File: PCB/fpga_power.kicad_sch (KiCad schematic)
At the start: 6 parts, among them U4 LFE5U-25F-6BG256C

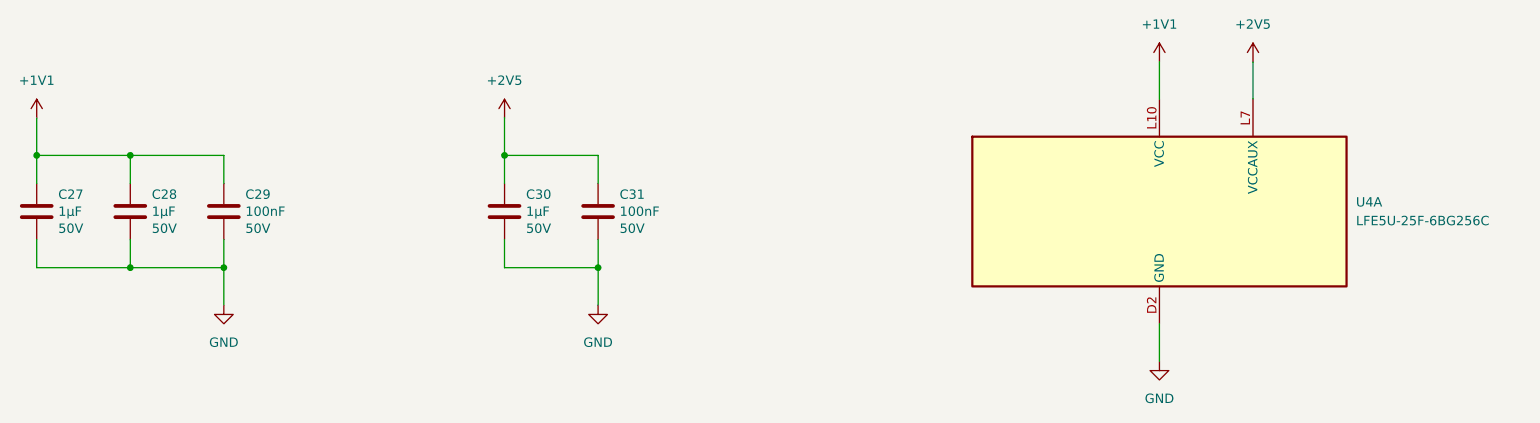
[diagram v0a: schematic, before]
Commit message: Add ESD protection
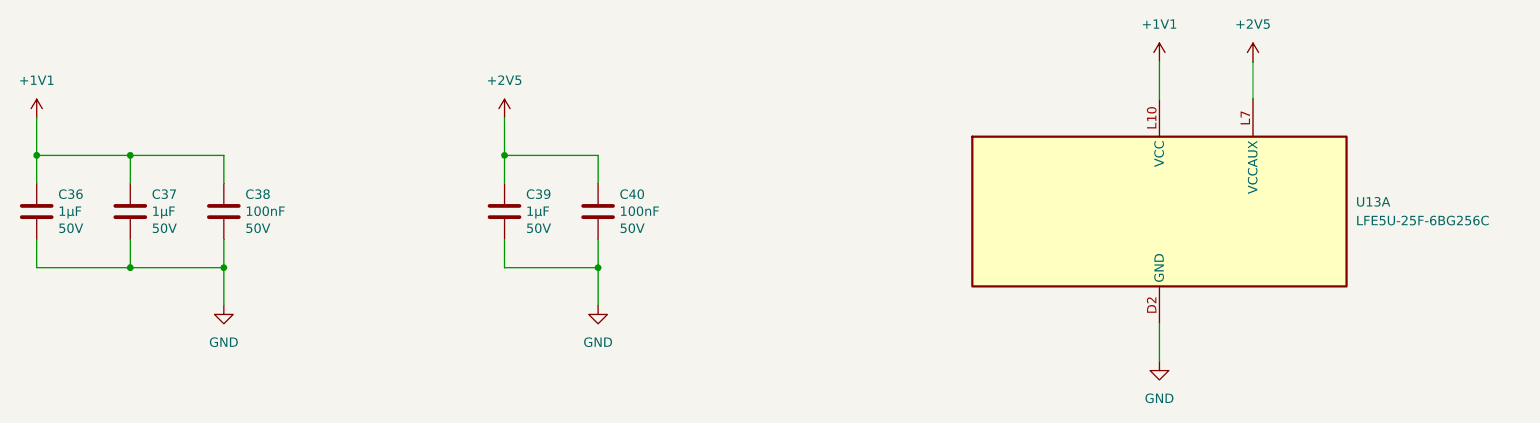
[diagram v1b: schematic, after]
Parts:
- renumbered C27 to C36, C28 to C37, C29 to C38, C30 to C39, C31 to C40, U4 to U13
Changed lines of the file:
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@@
 	(title_block
 		(title "Clavier - FPGA power")
-		(date "2025-06-01")
+		(date "2025-06-21")
 		(rev "1.0")
 		(company "Copyright (c) 2025 L. Sartory")
@@
 		(on_board yes)
 		(dnp no)
-		(property "Reference" "C27"
+		(property "Reference" "C36"
 			(at 53.721 86.5886 0)
 			(effects
@@
 			(project "clavier"
 				(path "/6362c6e0-59ef-40d3-b6e0-7e9dfe7b9b20/d73938da-f0ba-48e3-aac9-a36988c25c2c/e36c52fe-7af8-49a0-bf3c-a636c30fc9cb"
-					(reference "C27")
+					(reference "C36")
 					(unit 1)
 				)
@@
 		(on_board yes)
 		(dnp no)
-		(property "Reference" "C29"
+		(property "Reference" "C38"
 			(at 79.121 86.5886 0)
 			(effects
@@
 			(project "clavier"
 				(path "/6362c6e0-59ef-40d3-b6e0-7e9dfe7b9b20/d73938da-f0ba-48e3-aac9-a36988c25c2c/e36c52fe-7af8-49a0-bf3c-a636c30fc9cb"
-					(reference "C29")
+					(reference "C38")
 					(unit 1)
 				)
@@
 		(on_board yes)
 		(dnp no)
-		(property "Reference" "C28"
+		(property "Reference" "C37"
 			(at 66.421 86.5886 0)
 			(effects
@@
 			(project "clavier"
 				(path "/6362c6e0-59ef-40d3-b6e0-7e9dfe7b9b20/d73938da-f0ba-48e3-aac9-a36988c25c2c/e36c52fe-7af8-49a0-bf3c-a636c30fc9cb"
-					(reference "C28")
+					(reference "C37")
 					(unit 1)
 				)
@@
 		(on_board yes)
 		(dnp no)
-		(property "Reference" "C30"
+		(property "Reference" "C39"
 			(at 117.221 86.5886 0)
 			(effects
@@
 			(project "clavier"
 				(path "/6362c6e0-59ef-40d3-b6e0-7e9dfe7b9b20/d73938da-f0ba-48e3-aac9-a36988c25c2c/e36c52fe-7af8-49a0-bf3c-a636c30fc9cb"
-					(reference "C30")
+					(reference "C39")
 					(unit 1)
 				)
@@
 		(dnp no)
 		(fields_autoplaced yes)
-		(property "Reference" "U4"
+		(property "Reference" "U13"
 			(at 229.87 87.6299 0)
 			(effects
@@
 			(project "clavier"
 				(path "/6362c6e0-59ef-40d3-b6e0-7e9dfe7b9b20/d73938da-f0ba-48e3-aac9-a36988c25c2c/e36c52fe-7af8-49a0-bf3c-a636c30fc9cb"
-					(reference "U4")
+					(reference "U13")
 					(unit 1)
 				)
@@
 		(dnp no)
 		(fields_autoplaced yes)
-		(property "Reference" "#PWR057"
+		(property "Reference" "#PWR076"
 			(at 114.3 80.01 0)
 			(effects
@@
 			(project "clavier"
 				(path "/6362c6e0-59ef-40d3-b6e0-7e9dfe7b9b20/d73938da-f0ba-48e3-aac9-a36988c25c2c/e36c52fe-7af8-49a0-bf3c-a636c30fc9cb"
-					(reference "#PWR057")
+					(reference "#PWR076")
 					(unit 1)
 				)
@@
 		(dnp no)
 		(fields_autoplaced yes)
-		(property "Reference" "#PWR055"
+		(property "Reference" "#PWR074"
 			(at 215.9 72.39 0)
 			(effects
@@
 			(project "clavier"
 				(path "/6362c6e0-59ef-40d3-b6e0-7e9dfe7b9b20/d73938da-f0ba-48e3-aac9-a36988c25c2c/e36c52fe-7af8-49a0-bf3c-a636c30fc9cb"
-					(reference "#PWR055")
+					(reference "#PWR074")
 					(unit 1)
 				)
@@
 		(dnp no)
 		(fields_autoplaced yes)
-		(property "Reference" "#PWR054"
+		(property "Reference" "#PWR073"
 			(at 203.2 72.39 0)
 			(effects
@@
 			(project "clavier"
 				(path "/6362c6e0-59ef-40d3-b6e0-7e9dfe7b9b20/d73938da-f0ba-48e3-aac9-a36988c25c2c/e36c52fe-7af8-49a0-bf3c-a636c30fc9cb"
-					(reference "#PWR054")
+					(reference "#PWR073")
 					(unit 1)
 				)
@@
 		(dnp no)
 		(fields_autoplaced yes)
-		(property "Reference" "#PWR059"
+		(property "Reference" "#PWR078"
 			(at 127 107.95 0)
 			(effects
@@
 			(project "clavier"
 				(path "/6362c6e0-59ef-40d3-b6e0-7e9dfe7b9b20/d73938da-f0ba-48e3-aac9-a36988c25c2c/e36c52fe-7af8-49a0-bf3c-a636c30fc9cb"
-					(reference "#PWR059")
+					(reference "#PWR078")
 					(unit 1)
 				)
@@
 		(dnp no)
 		(fields_autoplaced yes)
-		(property "Reference" "#PWR058"
+		(property "Reference" "#PWR077"
 			(at 76.2 107.95 0)
 			(effects
@@
 			(project "clavier"
 				(path "/6362c6e0-59ef-40d3-b6e0-7e9dfe7b9b20/d73938da-f0ba-48e3-aac9-a36988c25c2c/e36c52fe-7af8-49a0-bf3c-a636c30fc9cb"
-					(reference "#PWR058")
+					(reference "#PWR077")
 					(unit 1)
 				)
@@
 		(dnp no)
 		(fields_autoplaced yes)
-		(property "Reference" "#PWR056"
+		(property "Reference" "#PWR075"
 			(at 50.8 80.01 0)
 			(effects
@@
 			(project "clavier"
 				(path "/6362c6e0-59ef-40d3-b6e0-7e9dfe7b9b20/d73938da-f0ba-48e3-aac9-a36988c25c2c/e36c52fe-7af8-49a0-bf3c-a636c30fc9cb"
-					(reference "#PWR056")
+					(reference "#PWR075")
 					(unit 1)
 				)
@@
 		(dnp no)
 		(fields_autoplaced yes)
-		(property "Reference" "#PWR060"
+		(property "Reference" "#PWR079"
 			(at 203.2 115.57 0)
 			(effects
@@
 			(project "clavier"
 				(path "/6362c6e0-59ef-40d3-b6e0-7e9dfe7b9b20/d73938da-f0ba-48e3-aac9-a36988c25c2c/e36c52fe-7af8-49a0-bf3c-a636c30fc9cb"
-					(reference "#PWR060")
+					(reference "#PWR079")
 					(unit 1)
 				)
@@
 		(on_board yes)
 		(dnp no)
-		(property "Reference" "C31"
+		(property "Reference" "C40"
 			(at 129.921 86.5886 0)
 			(effects
@@
 			(project "clavier"
 				(path "/6362c6e0-59ef-40d3-b6e0-7e9dfe7b9b20/d73938da-f0ba-48e3-aac9-a36988c25c2c/e36c52fe-7af8-49a0-bf3c-a636c30fc9cb"
-					(reference "C31")
+					(reference "C40")
 					(unit 1)
 				)

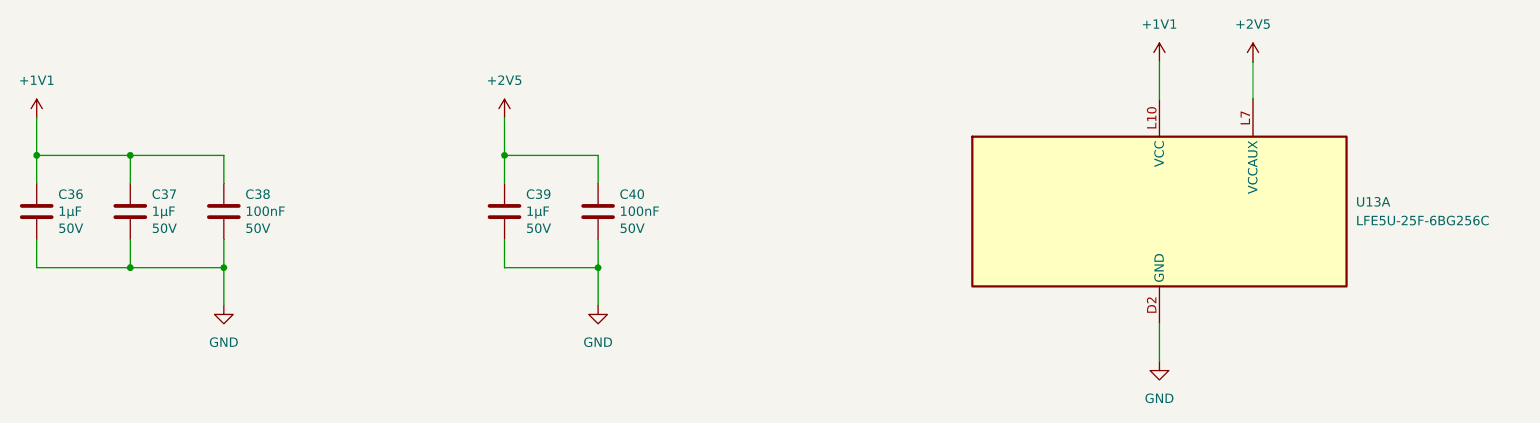
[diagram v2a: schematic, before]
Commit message: Complete the PCB routing
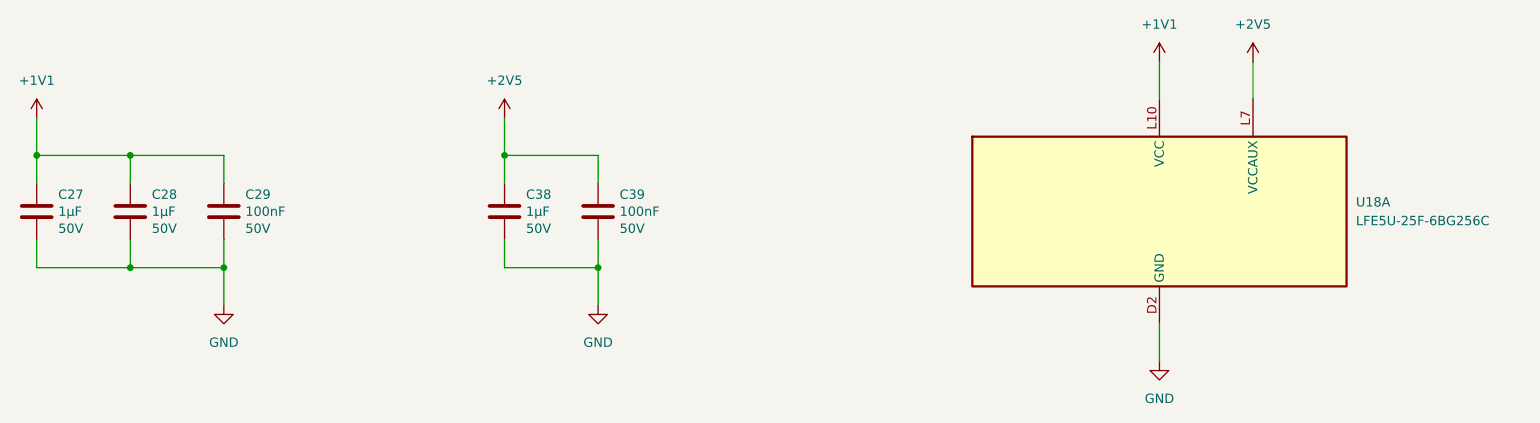
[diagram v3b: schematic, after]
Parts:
- renumbered C36 to C27, C37 to C28, C38 to C29, C39 to C38, C40 to C39, U13 to U18
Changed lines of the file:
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@@
 	(title_block
 		(title "Clavier - FPGA power")
-		(date "2025-06-21")
+		(date "2025-06-22")
 		(rev "1.0")
 		(company "Copyright (c) 2025 L. Sartory")
@@
 		(on_board yes)
 		(dnp no)
-		(property "Reference" "C36"
+		(property "Reference" "C27"
 			(at 53.721 86.5886 0)
 			(effects
@@
 			(project "clavier"
 				(path "/6362c6e0-59ef-40d3-b6e0-7e9dfe7b9b20/d73938da-f0ba-48e3-aac9-a36988c25c2c/e36c52fe-7af8-49a0-bf3c-a636c30fc9cb"
-					(reference "C36")
+					(reference "C27")
 					(unit 1)
 				)
@@
 		(on_board yes)
 		(dnp no)
-		(property "Reference" "C38"
+		(property "Reference" "C29"
 			(at 79.121 86.5886 0)
 			(effects
@@
 			(project "clavier"
 				(path "/6362c6e0-59ef-40d3-b6e0-7e9dfe7b9b20/d73938da-f0ba-48e3-aac9-a36988c25c2c/e36c52fe-7af8-49a0-bf3c-a636c30fc9cb"
-					(reference "C38")
+					(reference "C29")
 					(unit 1)
 				)
@@
 		(on_board yes)
 		(dnp no)
-		(property "Reference" "C37"
+		(property "Reference" "C28"
 			(at 66.421 86.5886 0)
 			(effects
@@
 			(project "clavier"
 				(path "/6362c6e0-59ef-40d3-b6e0-7e9dfe7b9b20/d73938da-f0ba-48e3-aac9-a36988c25c2c/e36c52fe-7af8-49a0-bf3c-a636c30fc9cb"
-					(reference "C37")
+					(reference "C28")
 					(unit 1)
 				)
@@
 		(on_board yes)
 		(dnp no)
-		(property "Reference" "C39"
+		(property "Reference" "C38"
 			(at 117.221 86.5886 0)
 			(effects
@@
 			(project "clavier"
 				(path "/6362c6e0-59ef-40d3-b6e0-7e9dfe7b9b20/d73938da-f0ba-48e3-aac9-a36988c25c2c/e36c52fe-7af8-49a0-bf3c-a636c30fc9cb"
-					(reference "C39")
+					(reference "C38")
 					(unit 1)
 				)
@@
 		(dnp no)
 		(fields_autoplaced yes)
-		(property "Reference" "U13"
+		(property "Reference" "U18"
 			(at 229.87 87.6299 0)
 			(effects
@@
 			(project "clavier"
 				(path "/6362c6e0-59ef-40d3-b6e0-7e9dfe7b9b20/d73938da-f0ba-48e3-aac9-a36988c25c2c/e36c52fe-7af8-49a0-bf3c-a636c30fc9cb"
-					(reference "U13")
+					(reference "U18")
 					(unit 1)
 				)
@@
 		(on_board yes)
 		(dnp no)
-		(property "Reference" "C40"
+		(property "Reference" "C39"
 			(at 129.921 86.5886 0)
 			(effects
@@
 			(project "clavier"
 				(path "/6362c6e0-59ef-40d3-b6e0-7e9dfe7b9b20/d73938da-f0ba-48e3-aac9-a36988c25c2c/e36c52fe-7af8-49a0-bf3c-a636c30fc9cb"
-					(reference "C40")
+					(reference "C39")
 					(unit 1)
 				)
